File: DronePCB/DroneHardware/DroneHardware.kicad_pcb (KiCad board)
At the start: 2 copper layers, 48 parts, among them J201 USB_B_Mini, J202 BATTERY, J203 I2C_CONN, J204 SWD_CONN, J205 USART6_CONN, Q101 AO3401A, SW1 SW_SPDT, U1 STM32F401RCT6, U101 MP2359DJ-LF-Z, U201 USBLC6-2SC6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

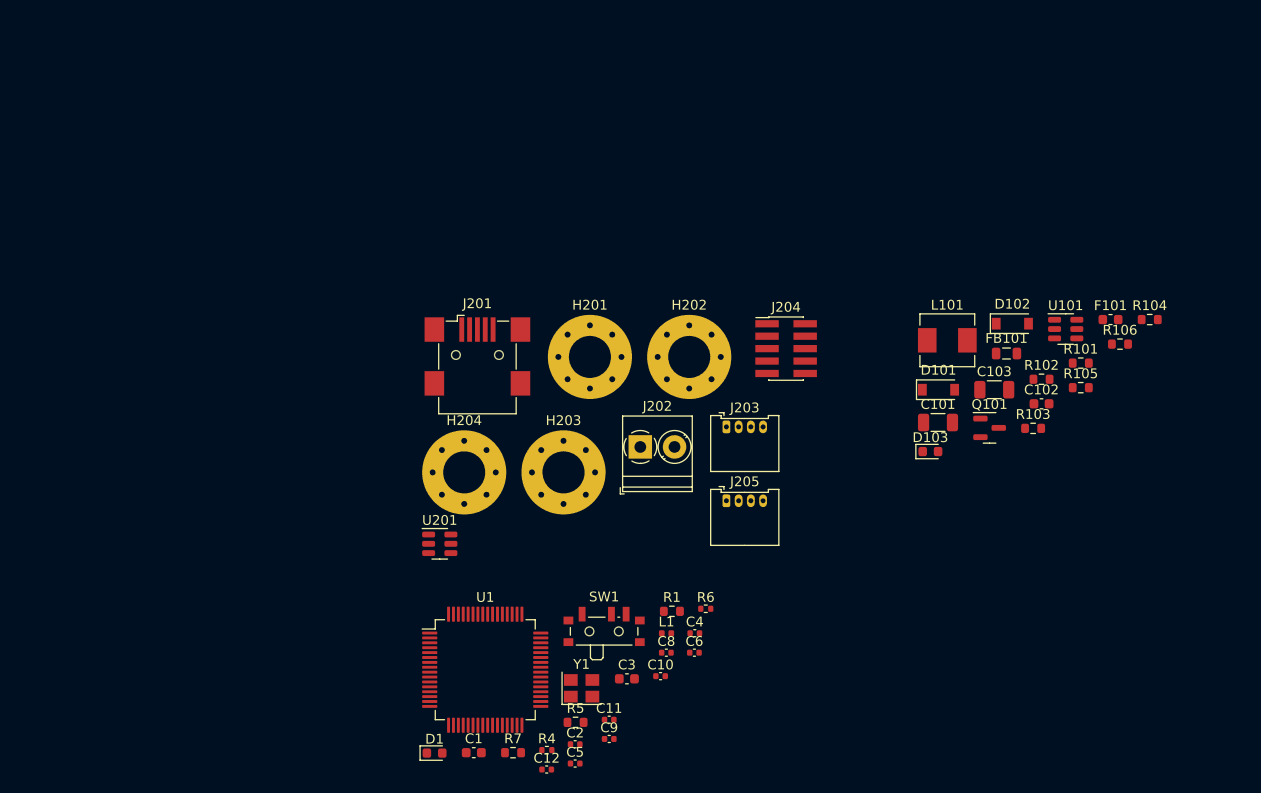
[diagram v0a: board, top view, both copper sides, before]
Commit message: Aggiornamento Aggiunta della MPU-6050 per test
E' stato fatto uno studio per capire il funzionamento di OMNIBUSF4
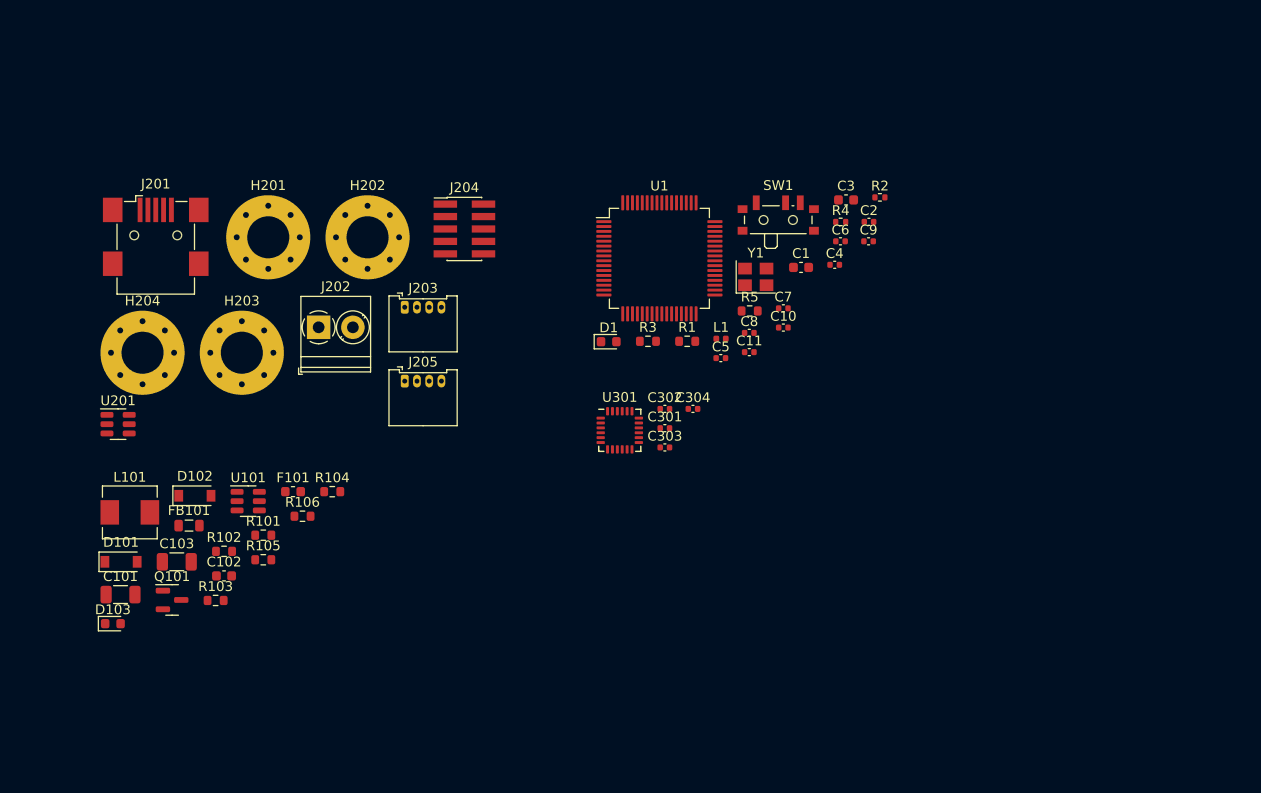
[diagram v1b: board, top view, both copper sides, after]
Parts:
- removed C12: 12p, Capacitor_SMD:C_0402_1005Metric
- removed R6: 47, Resistor_SMD:R_0402_1005Metric
- removed R7: 2k2, Resistor_SMD:R_0603_1608Metric
- added C301: 10n, Capacitor_SMD:C_0402_1005Metric, F.Cu at (137.3, 80.2)
- added C302: 100n, Capacitor_SMD:C_0402_1005Metric, F.Cu at (137.3, 78.3)
- added C303: 100n, Capacitor_SMD:C_0402_1005Metric, F.Cu at (137.3, 82.2)
- added C304: 22n, Capacitor_SMD:C_0402_1005Metric, F.Cu at (140.2, 78.3)
- added C7: 100n, Capacitor_SMD:C_0402_1005Metric, F.Cu at (149.4, 68.0)
- added R2: 10K, Resistor_SMD:R_0402_1005Metric, F.Cu at (159.3, 56.6)
- added R3: 2k2, Resistor_SMD:R_0603_1608Metric, F.Cu at (135.6, 71.3)
- added U301: MPU-6050, Sensor_Motion:InvenSense_QFN-24_4x4mm_P0.5mm, F.Cu at (132.7, 80.5)
- C10: value 12p -> 10n
- C11: value 10n -> 12p
- C8: value 100n -> 1u
- C9: value 1u -> 12p
- R4: value 10K -> 47
- moved L101 85.4 mm to (82.6, 88.8)
- moved C102 85.4 mm to (92.2, 95.3)
- moved D101 85.4 mm to (81.7, 93.9)
- moved Q101 85.4 mm to (86.9, 97.8)
- moved R101 85.4 mm to (96.3, 91.2)
- moved R102 85.4 mm to (92.2, 92.8)
- moved R104 85.4 mm to (103.3, 86.7)
- moved R105 85.4 mm to (96.3, 93.7)
- moved U101 85.4 mm to (94.7, 87.7)
- moved C101 85.4 mm to (81.7, 97.2)
- moved C103 85.4 mm to (87.4, 93.9)
- moved D102 85.4 mm to (89.3, 87.1)
- moved D103 85.4 mm to (80.9, 100.2)
- moved F101 85.4 mm to (99.3, 86.7)
- moved FB101 85.4 mm to (88.7, 90.2)
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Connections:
- C10 pad 1: HSE_IN -> +3.3VA
- C11 pad 1: +3.3VA -> Net-(C11-Pad1)
- C8 pad 1: BUCK_VOUT_3V3 -> +3.3VA
- C9 pad 1: +3.3VA -> HSE_IN
- R4 pad 1: BOOT0 -> HSE_OUT
- R4 pad 2: Net-(R4-Pad2) -> Net-(C11-Pad1)
- R5 pad 2: I2C1_SCL -> I2C1_SDA
- SW1 pad 2: Net-(R4-Pad2) -> Net-(R2-Pad2)
- U1 pad 57: unconnected-(U1-Pad57) -> GYRO_INT
- Y1 pad 3: Net-(C12-Pad1) -> Net-(C11-Pad1)

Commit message: Creazione PCB e utilizzo di processore STM32F405
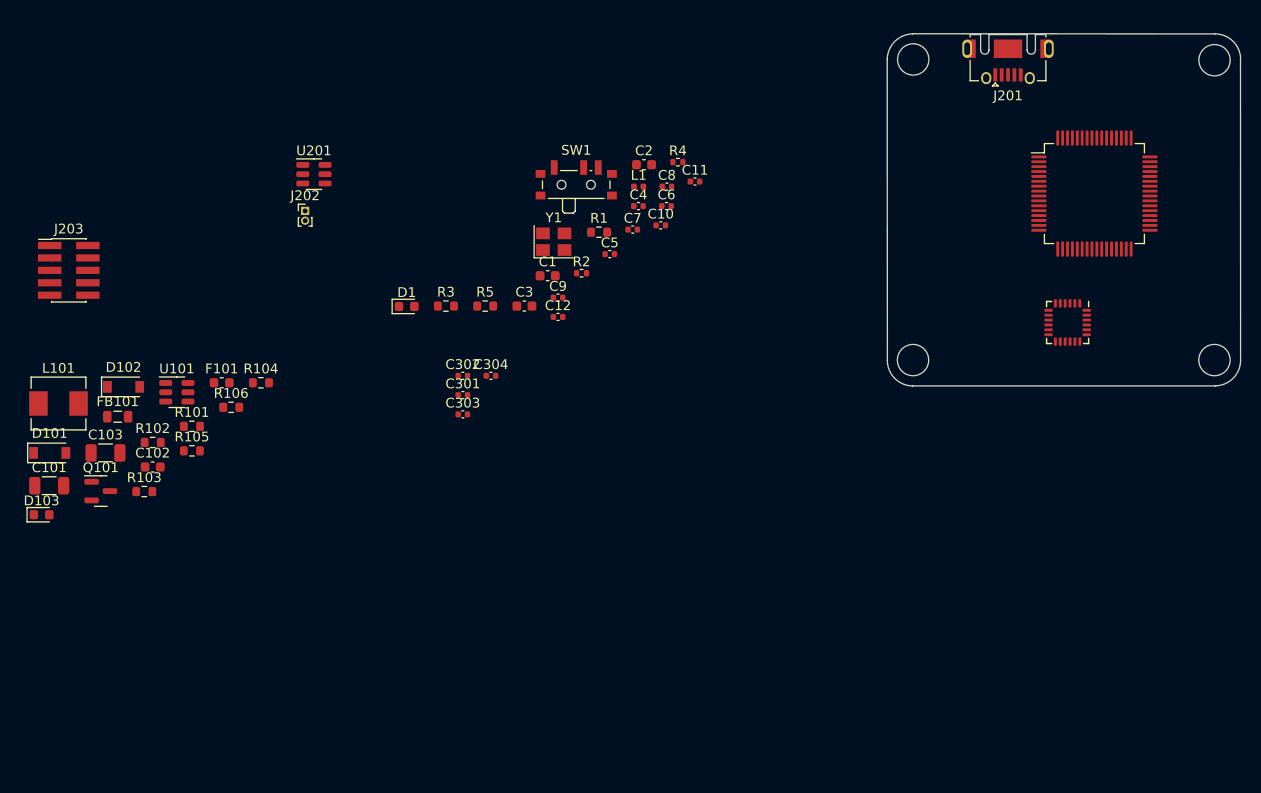
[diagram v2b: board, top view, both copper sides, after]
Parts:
- removed J204: SWD_CONN, Connector_PinHeader_1.27mm:PinHeader_2x05_P1.27mm_Vertical_SMD
- removed J205: USART6_CONN, Connector_Molex:Molex_PicoBlade_53048-0410_1x04_P1.25mm_Horizontal
- added C12: 12p, Capacitor_SMD:C_0402_1005Metric, F.Cu at (126.4, 68.9)
- C1: value 4u7 -> 2u2
- C10: value 10n -> 12p
- C11: value 12p -> 10n
- C2: value 100n -> 2u2; footprint Capacitor_SMD:C_0402_1005Metric -> Capacitor_SMD:C_0603_1608Metric
- C3: value 2u2 -> 4u7
- C8: value 1u -> 100n
- C9: value 12p -> 1u
- H201, H202, H203, H204: footprint MountingHole:MountingHole_4.3mm_M4_Pad_Via -> MountingHole:MountingHole_3.2mm_M3
- J201: value USB_B_Mini -> USB_B_Micro; footprint Connector_USB:USB_Mini-B_Wuerth_65100516121_Horizontal -> Connector_USB:USB_Micro-AB_Molex_47590-0001
- J202: footprint TerminalBlock_Phoenix:TerminalBlock_Phoenix_PT-1,5-2-3.5-H_1x02_P3.50mm_Horizontal -> Connector_PinHeader_1.00mm:PinHeader_1x02_P1.00mm_Vertical
- J203: value I2C_CONN -> SWD_CONN; footprint Connector_Molex:Molex_PicoBlade_53048-0410_1x04_P1.25mm_Horizontal -> Connector_PinHeader_1.27mm:PinHeader_2x05_P1.27mm_Vertical_SMD
- U1: value STM32F401RCT6 -> STM32F405RGT6
- moved H203 103.8 mm to (193.5, 42.6)
- moved H201 97.5 mm to (193.5, 73.3)
- moved J201 89.2 mm to (172.4, 41.5), turned to 180 degrees
- moved H204 84.3 mm to (162.7, 42.5)
- moved H202 57.2 mm to (162.7, 73.3)
- moved U301 47.1 mm to (178.5, 69.4), turned to -90 degrees
- moved U1 45.0 mm to (181.2, 56.2)
- moved C3 34.6 mm to (122.9, 67.8)
- moved J203 34.5 mm to (76.4, 64.1)
- moved U201 32.5 mm to (101.4, 54.3)
- moved C9 32.3 mm to (126.4, 66.9)
- moved R2 31.5 mm to (128.8, 64.4)
- moved R5 27.0 mm to (118.9, 67.8)
- moved C1 25.9 mm to (125.3, 64.7)
- moved C2 23.7 mm to (135.2, 53.3)
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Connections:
- C1 pad 1: BUCK_VOUT_3V3 -> Net-(C1-Pad1)
- C10 pad 1: +3.3VA -> HSE_IN
- C11 pad 1: Net-(C11-Pad1) -> +3.3VA
- C2 pad 1: BUCK_VOUT_3V3 -> Net-(C2-Pad1)
- C3 pad 1: Net-(C3-Pad1) -> BUCK_VOUT_3V3
- C8 pad 1: +3.3VA -> BUCK_VOUT_3V3
- C9 pad 1: HSE_IN -> +3.3VA
- D1 pad 2: LED_STATUS -> LED0
- J203 pad 2: I2C1_SCL -> SWDIO
- J203 pad 3: I2C1_SDA -> GND
- J203 pad 4: GND -> SWCLK
- R4 pad 2: Net-(C11-Pad1) -> Net-(C12-Pad1)
- U1 pad 13: +3.3VA -> BUCK_VOUT_3V3
- U1 pad 16: LED_STATUS -> unconnected-(U1-Pad16)
- U1 pad 24: unconnected-(U1-Pad24) -> GYRO_INT_EXTI
- U1 pad 30: Net-(C3-Pad1) -> unconnected-(U1-Pad30)
- U1 pad 31: GND -> Net-(C1-Pad1)
- U1 pad 37: USART6_TX -> unconnected-(U1-Pad37)
- U1 pad 38: USART6_RX -> unconnected-(U1-Pad38)
- U1 pad 47: GND -> Net-(C2-Pad1)
- U1 pad 57: GYRO_INT -> LED0
- U1 pad 58: I2C1_SCL -> unconnected-(U1-Pad58)
- U1 pad 59: I2C1_SDA -> unconnected-(U1-Pad59)
- U1 pad 61: unconnected-(U1-Pad61) -> I2C1_SCL
- U1 pad 62: unconnected-(U1-Pad62) -> I2C1_SDA
- U301 pad 12: GYRO_INT -> GYRO_INT_EXTI
- Y1 pad 3: Net-(C11-Pad1) -> Net-(C12-Pad1)
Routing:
- added copper zone on In2.Cu, net BUCK_VOUT_3V3
- added copper zone on In1.Cu, net GND
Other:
- board outline added: 36.1 x 36 mm
- copper layers 2 -> 4

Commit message: Creazione dei bordi della scheda e posizionamento dei componenti importanti
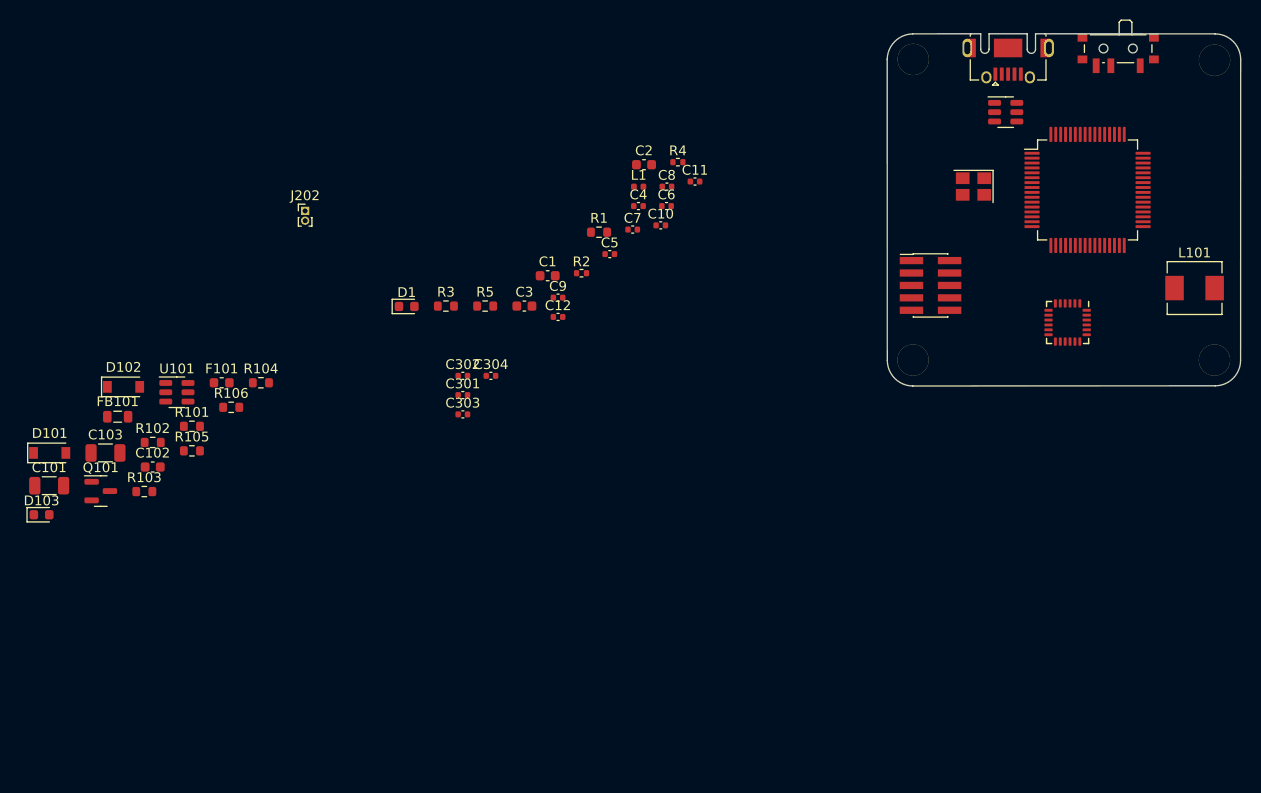
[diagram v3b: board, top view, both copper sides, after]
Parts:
- moved L101 116.7 mm to (191.4, 65.9)
- moved J203 88.1 mm to (164.5, 65.6)
- moved U201 71.0 mm to (172.1, 47.9)
- moved SW1 57.0 mm to (183.6, 41.8), turned to 180 degrees
- moved Y1 43.3 mm to (168.8, 55.5), turned to 180 degrees
- moved U1 0.79 mm to (180.5, 55.9)
- moved J201 0.08 mm to (172.4, 41.4)
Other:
- outline, holes or cut-outs redrawn

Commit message: Modifica della porta USB
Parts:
- J201: footprint Connector_USB:USB_Micro-AB_Molex_47590-0001 -> Connector_USB:USB_Micro-B_Molex-105017-0001
- moved J201 1.21 mm to (172.5, 42.6)
- turned U201 to -90 degrees
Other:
- outline, holes or cut-outs redrawn

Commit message: Utilizzo di mpu-6000
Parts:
- removed C304: 22n, Capacitor_SMD:C_0402_1005Metric
- C301: value 10n -> 100n
- C303: value 100n -> 22n
- U301: value MPU-6050 -> MPU-6000
- moved C301 30.6 mm to (144.8, 88.9)
- moved C302 28.9 mm to (141.9, 88.9)
- moved C303 28.0 mm to (141.9, 90.9)
- moved U301 1.82 mm to (177.8, 71.1)
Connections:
- C302 pad 1: BUCK_VOUT_3V3 -> Net-(C302-Pad1)
- U301 pad 10: Net-(C303-Pad1) -> Net-(C302-Pad1)
- U301 pad 14: unconnected-(U301-Pad14) -> (no net)
- U301 pad 15: unconnected-(U301-Pad15) -> (no net)
- U301 pad 16: unconnected-(U301-Pad16) -> (no net)
- U301 pad 17: unconnected-(U301-Pad17) -> (no net)
- U301 pad 19: unconnected-(U301-Pad19) -> (no net)
- U301 pad 2: unconnected-(U301-Pad2) -> (no net)
- U301 pad 20: Net-(C304-Pad1) -> Net-(C303-Pad1)
- U301 pad 21: unconnected-(U301-Pad21) -> (no net)
- U301 pad 22: unconnected-(U301-Pad22) -> (no net)
- U301 pad 3: unconnected-(U301-Pad3) -> (no net)
- U301 pad 4: unconnected-(U301-Pad4) -> (no net)
- U301 pad 5: unconnected-(U301-Pad5) -> (no net)
- U301 pad 8: BUCK_VOUT_3V3 -> GND

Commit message: Collegamento corretto di mpu-6000
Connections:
- U1 pad 20: unconnected-(U1-Pad20) -> MPU6000_CS_PIN
- U1 pad 21: unconnected-(U1-Pad21) -> GYRO_SCK_PIN
- U1 pad 22: unconnected-(U1-Pad22) -> GYRO_MISO_PIN
- U1 pad 23: unconnected-(U1-Pad23) -> GYRO_MOSI_PIN
- U1 pad 61: I2C1_SCL -> unconnected-(U1-Pad61)
- U1 pad 62: I2C1_SDA -> unconnected-(U1-Pad62)
- U301 pad 23: I2C1_SCL -> GYRO_SCK_PIN
- U301 pad 24: I2C1_SDA -> GYRO_MOSI_PIN
- U301 pad 8: GND -> MPU6000_CS_PIN
- U301 pad 9: GND -> GYRO_MISO_PIN

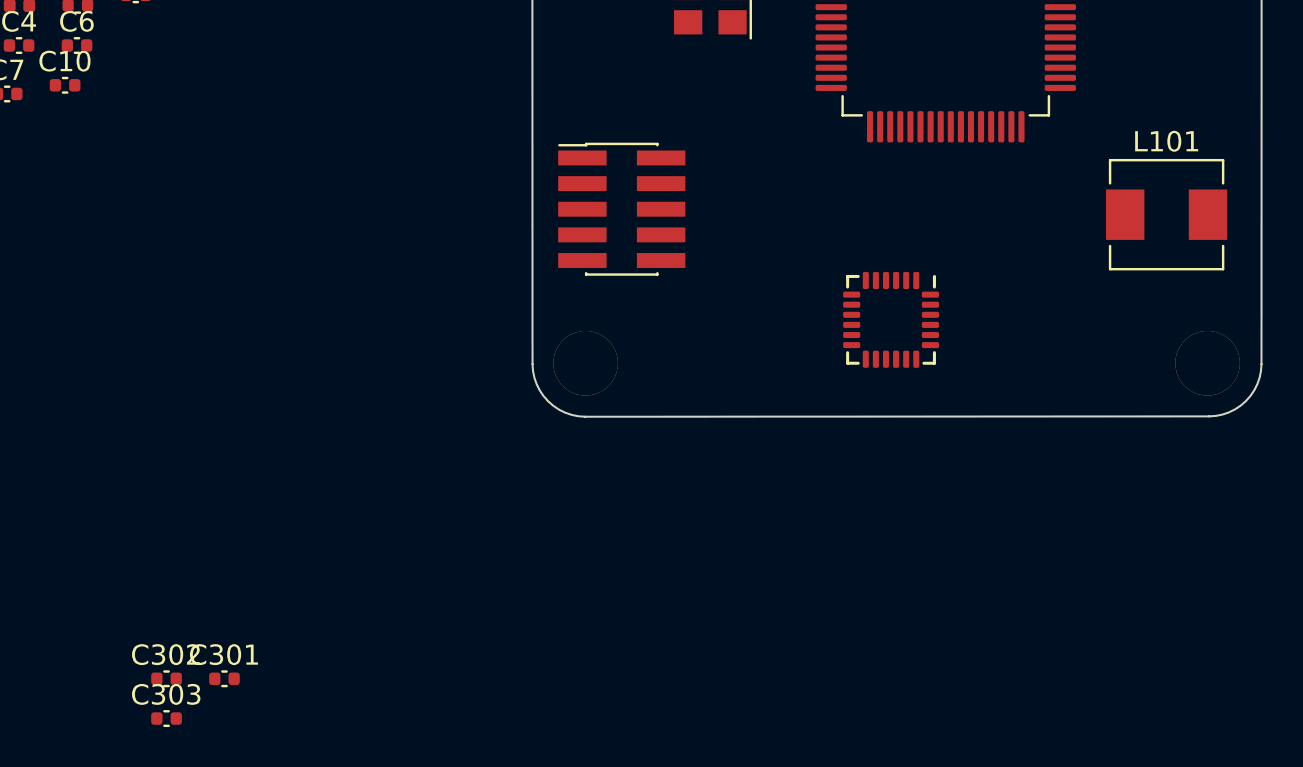
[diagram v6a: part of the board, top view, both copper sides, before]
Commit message: Collegamento fisico di MPU-6000
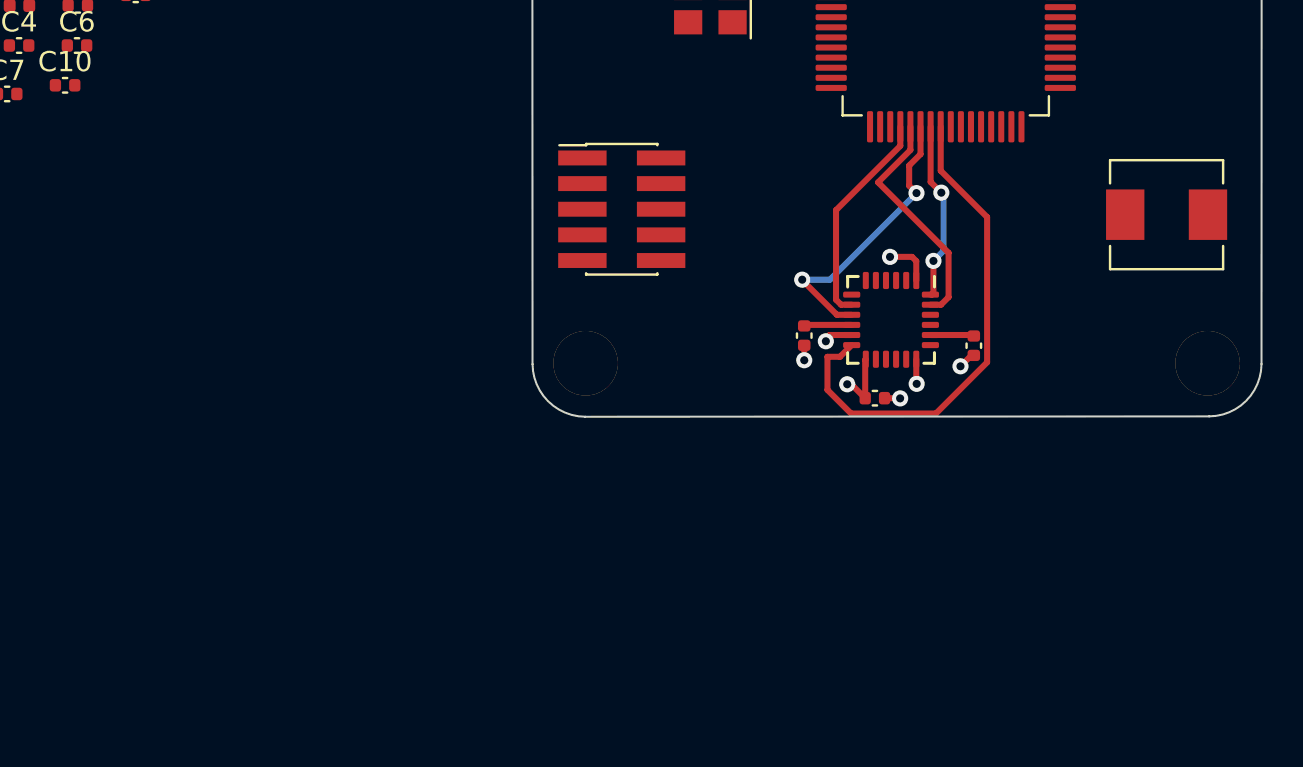
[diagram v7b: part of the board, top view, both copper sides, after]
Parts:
- moved C303 44.0 mm to (181.9, 72.4), turned to -90 degrees
- moved C302 35.9 mm to (173.5, 71.9), turned to -90 degrees
- moved C301 35.1 mm to (177.0, 75.0)
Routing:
- net GYRO_INT_EXTI: track 0.00 -> 25.1 mm
- net GYRO_MISO_PIN: track 0.00 -> 14.3 mm, vias 0 -> 2
- net GYRO_SCK_PIN: track 0.00 -> 11.6 mm
- net MPU6000_CS_PIN: track 0.00 -> 10.8 mm
- net GYRO_MOSI_PIN: track 0.00 -> 8.90 mm, vias 0 -> 2
- net GND: track 0.00 -> 7.31 mm, vias 0 -> 6
- net BUCK_VOUT_3V3: track 0.00 -> 3.12 mm, vias 0 -> 1
- net Net-(C302-Pad1): track 0.00 -> 2.37 mm
- net Net-(C303-Pad1): track 0.00 -> 2.17 mm

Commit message: Miglioramento delle connessioni
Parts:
- moved D1 80.8 mm to (188.5, 45.2), turned to 180 degrees
- moved R1 61.1 mm to (189.1, 42.7), turned to -90 degrees
- moved C5 57.8 mm to (188.5, 51.6), turned to 90 degrees
- moved R2 55.4 mm to (181.2, 46.3), turned to 90 degrees
- moved C4 50.1 mm to (184.3, 63.9), turned to -90 degrees
- moved C6 40.2 mm to (176.6, 48.5)
- moved C8 40.1 mm to (176.9, 63.4), turned to 180 degrees
- moved C7 39.3 mm to (172.5, 52.1), turned to 180 degrees
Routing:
- net BUCK_VOUT_3V3: track 3.12 -> 14.4 mm, vias 1 -> 2
- net LED0: track 0.00 -> 10.6 mm
- net GND: track 7.31 -> 16.1 mm, vias 6 -> 12
- net GYRO_INT_EXTI: track 25.1 -> 18.9 mm, vias 0 -> 2
- net BOOT0: track 0.00 -> 4.41 mm
- net Net-(R2-Pad2): track 0.00 -> 3.42 mm
- net GYRO_MISO_PIN: track 14.3 -> 12.4 mm
- net Net-(D1-Pad1): track 0.00 -> 1.73 mm
- net GYRO_SCK_PIN: track 11.6 -> 10.3 mm
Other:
- copper layers 4 -> 6
